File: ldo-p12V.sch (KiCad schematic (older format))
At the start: 8 parts

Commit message: change LDO sch capacitors & finish component selection
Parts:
- removed C?: 22u, symbol Device:C
- added C?: 4.7u, Capacitor_SMD:C_0805_2012Metric_Pad1.15x1.40mm_HandSolder, symbol Device:C
- C?: footprint (none) -> Capacitor_SMD:C_0805_2012Metric_Pad1.15x1.40mm_HandSolder; Description (none) -> CAP CER 10UF 16V X5R 0805; Manufacturer (none) -> Taiyo Yuden; Manufacturer Part Number (none) -> EMK212ABJ106KD-T; Supplier (none) -> Digi-Key; Supplier Part Number (none) -> 587-2980-1-ND
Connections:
- net +12Vreg: now also C?.2
- net GND: now also C?.1
- net at R?.2, U?.8 (SET): now also C?.2; no longer C?.2
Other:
- moved on the sheet: C?
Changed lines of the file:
@@
 L Device:C C?
 U 1 1 5CA5D41C
-P 4350 4400
+P 6650 4150
 AR Path="/5C87B3B6/5CA5D41C" Ref="C?"  Part="1"
 AR Path="/5CA59CF7/5CA5D41C" Ref="C?"  Part="1"
-F 0 "C?" H 4235 4354 50  0000 R CNN
-F 1 "10u" H 4235 4445 50  0000 R CNN
-F 2 "" H 4388 4250 50  0001 C CNN
-F 3 "" H 4350 4400 50  0001 C CNN
-F 4 "" H 1900 -750 50  0001 C CNN "Description"
-F 5 "" H 1900 -750 50  0001 C CNN "Manufacturer"
-F 6 "" H 1900 -750 50  0001 C CNN "Manufacturer Part Number"
-F 7 "" H 1900 -750 50  0001 C CNN "Supplier"
-F 8 "" H 1900 -750 50  0001 C CNN "Supplier Part Number"
-	1    4350 4400
-	1    0    0    1
+F 0 "C?" H 6535 4104 50  0000 R CNN
+F 1 "10u" H 6535 4195 50  0000 R CNN
+F 2 "Capacitor_SMD:C_0805_2012Metric_Pad1.15x1.40mm_HandSolder" H 6688 4000 50  0001 C CNN
+F 3 "https://www.yuden.co.jp/productdata/catalog/mlcc07_e.pdf" H 6650 4150 50  0001 C CNN
+F 4 "CAP CER 10UF 16V X5R 0805" H 4200 -1000 50  0001 C CNN "Description"
+F 5 "Taiyo Yuden" H 4200 -1000 50  0001 C CNN "Manufacturer"
+F 6 "EMK212ABJ106KD-T" H 4200 -1000 50  0001 C CNN "Manufacturer Part Number"
+F 7 "Digi-Key" H 4200 -1000 50  0001 C CNN "Supplier"
+F 8 "587-2980-1-ND" H 4200 -1000 50  0001 C CNN "Supplier Part Number"
+	1    6650 4150
+	-1   0    0    1
 $EndComp
 Wire Wire Line
@@
 Wire Wire Line
 	6450 4650 5500 4650
-$Comp
-L Device:C C?
-U 1 1 5CA5F77A
-P 6650 4150
-AR Path="/5C87B3B6/5CA5F77A" Ref="C?"  Part="1"
-AR Path="/5CA59CF7/5CA5F77A" Ref="C?"  Part="1"
-F 0 "C?" H 6535 4104 50  0000 R CNN
-F 1 "22u" H 6535 4195 50  0000 R CNN
-F 2 "" H 6688 4000 50  0001 C CNN
-F 3 "" H 6650 4150 50  0001 C CNN
-F 4 "" H 4200 -1000 50  0001 C CNN "Description"
-F 5 "" H 4200 -1000 50  0001 C CNN "Manufacturer"
-F 6 "" H 4200 -1000 50  0001 C CNN "Manufacturer Part Number"
-F 7 "" H 4200 -1000 50  0001 C CNN "Supplier"
-F 8 "" H 4200 -1000 50  0001 C CNN "Supplier Part Number"
-	1    6650 4150
-	-1   0    0    1
-$EndComp
 Wire Wire Line
 	6450 3650 6650 3650
@@
 	3950 4650 4350 4650
 Connection ~ 4350 4650
+$Comp
+L Device:C C?
+U 1 1 5D0393AC
+P 4350 4400
+AR Path="/5C87B3B6/5D0393AC" Ref="C?"  Part="1"
+AR Path="/5C903B7C/5D0393AC" Ref="C?"  Part="1"
+F 0 "C?" H 4235 4354 50  0000 R CNN
+F 1 "4.7u" H 4235 4445 50  0000 R CNN
+F 2 "Capacitor_SMD:C_0805_2012Metric_Pad1.15x1.40mm_HandSolder" H 4388 4250 50  0001 C CNN
+F 3 "https://www.yuden.co.jp/productdata/catalog/mlcc01_e.pdf" H 4350 4400 50  0001 C CNN
+F 4 "CAP CER 4.7UF 10V X5R 0805" H 1050 850 50  0001 C CNN "Description"
+F 5 "Taiyo Yuden" H 1050 850 50  0001 C CNN "Manufacturer"
+F 6 "LMK212BJ475KD-T" H 1050 850 50  0001 C CNN "Manufacturer Part Number"
+F 7 "Digi-Key" H 1050 850 50  0001 C CNN "Supplier"
+F 8 "587-1297-1-ND" H 1050 850 50  0001 C CNN "Supplier Part Number"
+	1    4350 4400
+	1    0    0    1
+$EndComp
 $EndSCHEMATC

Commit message: add components for audo.sch
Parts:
- R?: Description RES SMD 121K OHM 0.1% 1/8W 0805 Thin Film -> RES SMD 121K OHM 0.1% 1/8W 0805 Metal Film
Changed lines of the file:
@@
 F 2 "Resistor_SMD:R_0805_2012Metric_Pad1.15x1.40mm_HandSolder" V 4480 4400 50  0001 C CNN
 F 3 "https://industrial.panasonic.com/cdbs/www-data/pdf/RDM0000/AOA0000C307.pdf" H 4550 4400 50  0001 C CNN
-F 4 "RES SMD 121K OHM 0.1% 1/8W 0805 Thin Film" H 4550 4400 50  0001 C CNN "Description"
+F 4 "RES SMD 121K OHM 0.1% 1/8W 0805 Metal Film" H 4550 4400 50  0001 C CNN "Description"
 F 5 "Panasonic Electronic Components" H 4550 4400 50  0001 C CNN "Manufacturer"
 F 6 "ERA-6AEB1213V" H 4550 4400 50  0001 C CNN "Manufacturer Part Number"

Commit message: switch components supplier to Mouser for price/availability
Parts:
- C?: Supplier Digi-Key -> Mouser; Supplier Part Number 587-1297-1-ND -> 963-LMK212BJ475KD-T
- U?: Supplier Digi-Key -> Mouser; Supplier Part Number LT3045EMSE#PBF-ND -> 584-LT3045EMSE#PBF
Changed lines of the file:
@@
 F 5 "Linear Technology" H 0   0   50  0001 C CNN "Manufacturer"
 F 6 "LT3045EMSE#PBF" H 0   0   50  0001 C CNN "Manufacturer Part Number"
-F 7 "Digi-Key" H 0   0   50  0001 C CNN "Supplier"
-F 8 "LT3045EMSE#PBF-ND" H 0   0   50  0001 C CNN "Supplier Part Number"
+F 7 "Mouser" H 0   0   50  0001 C CNN "Supplier"
+F 8 "584-LT3045EMSE#PBF" H 0   0   50  0001 C CNN "Supplier Part Number"
 	1    5500 3900
 	1    0    0    -1
@@
 F 5 "Taiyo Yuden" H 1050 850 50  0001 C CNN "Manufacturer"
 F 6 "LMK212BJ475KD-T" H 1050 850 50  0001 C CNN "Manufacturer Part Number"
-F 7 "Digi-Key" H 1050 850 50  0001 C CNN "Supplier"
-F 8 "587-1297-1-ND" H 1050 850 50  0001 C CNN "Supplier Part Number"
+F 7 "Mouser" H 1050 850 50  0001 C CNN "Supplier"
+F 8 "963-LMK212BJ475KD-T" H 1050 850 50  0001 C CNN "Supplier Part Number"
 	1    4350 4400
 	1    0    0    1

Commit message: update ldo threshold configs & components
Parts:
- R?: value 1.82M -> 1.91M; Description RES SMD 1.82M OHM 1% 1/8W 0805 -> RES SMD 1.91M OHM 1% 1/8W 0805; Manufacturer Part Number ERJ-6ENF1824V -> ERJ-6ENF1914V; Supplier Part Number P1.82BTCT-ND -> P1.91BTCT-ND
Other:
- note added: "LT3045 keeps IC in shutdown while EN is below 1.24V\n—> V_EN_threshold = 1.24V*(1+(432k/49.9k)) = 11.975V\n\nLT3045 fast start-up circuitry increases SET pin\ncurrent to ~~2mA while PGFB is below 300mV.\n—> V_PG_threshold = 0.3V*(1+(1.91M/49.9k)) = 11.78V"
- note removed: "NOTE: LT3045’s fast start-up circuitry increases the\nSET pin current to ~2mA while PGFB is below 300mV."
- note removed: "R_PG values of 1.13M & 29.4k yield fast start-up lasting ~~50ms"
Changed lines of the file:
@@
 AR Path="/5CA59CF7/5CA5DDF4" Ref="R?"  Part="1"
 F 0 "R?" V 6530 3900 50  0000 C CNN
-F 1 "1.82M" V 6450 3900 50  0000 C CNN
+F 1 "1.91M" V 6450 3900 50  0000 C CNN
 F 2 "Resistor_SMD:R_0805_2012Metric_Pad1.15x1.40mm_HandSolder" V 6380 3900 50  0001 C CNN
 F 3 "https://industrial.panasonic.com/cdbs/www-data/pdf/RDA0000/AOA0000C304.pdf" H 6450 3900 50  0001 C CNN
-F 4 "RES SMD 1.82M OHM 1% 1/8W 0805" H 6450 3900 50  0001 C CNN "Description"
+F 4 "RES SMD 1.91M OHM 1% 1/8W 0805" H 6450 3900 50  0001 C CNN "Description"
 F 5 "Panasonic Electronic Components" H 6450 3900 50  0001 C CNN "Manufacturer"
-F 6 "ERJ-6ENF1824V" H 6450 3900 50  0001 C CNN "Manufacturer Part Number"
+F 6 "ERJ-6ENF1914V" H 6450 3900 50  0001 C CNN "Manufacturer Part Number"
 F 7 "Digi-Key" H 6450 3900 50  0001 C CNN "Supplier"
-F 8 "P1.82BTCT-ND" H 6450 3900 50  0001 C CNN "Supplier Part Number"
+F 8 "P1.91BTCT-ND" H 6450 3900 50  0001 C CNN "Supplier Part Number"
 	1    6450 3900
 	-1   0    0    1
@@
 	6850 3650 6650 3650
 Connection ~ 6650 3650
-Text Notes 3900 5400 0    50   ~ 0
-NOTE: LT3045’s fast start-up circuitry increases the\nSET pin current to ~2mA while PGFB is below 300mV.
-Text Notes 3900 5550 0    50   ~ 0
-R_PG values of 1.13M & 29.4k yield fast start-up lasting ~~50ms
+Text Notes 3950 3450 0    50   ~ 0
+LT3045 keeps IC in shutdown while EN is below 1.24V\n—> V_EN_threshold = 1.24V*(1+(432k/49.9k)) = 11.975V\n\nLT3045 fast start-up circuitry increases SET pin\ncurrent to ~~2mA while PGFB is below 300mV.\n—> V_PG_threshold = 0.3V*(1+(1.91M/49.9k)) = 11.78V
 $Comp
 L Device:R R?

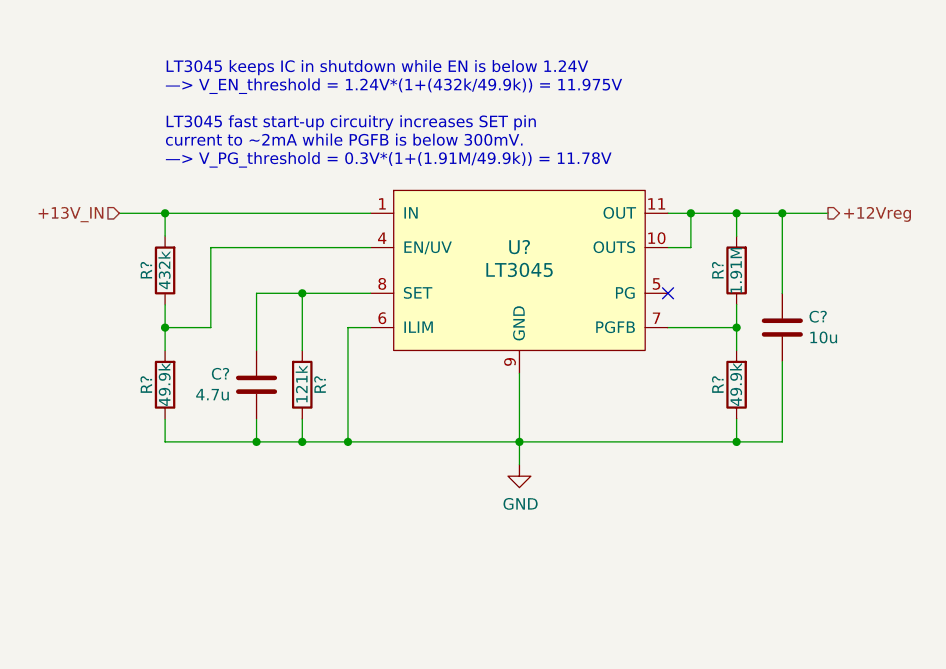
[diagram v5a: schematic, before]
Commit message: fix audio pot label & other label sizing
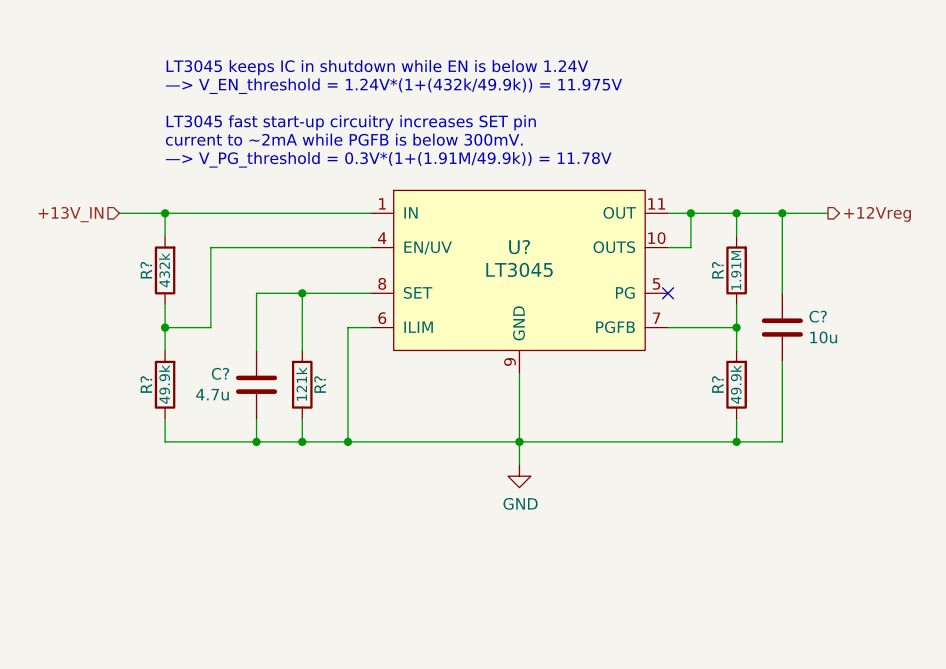
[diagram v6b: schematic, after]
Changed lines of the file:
@@
 AR Path="/5CA59CF7/5CA5D410" Ref="R?"  Part="1"
 F 0 "R?" V 4630 4400 50  0000 C CNN
-F 1 "121k" V 4550 4400 50  0000 C CNN
+F 1 "121k" V 4550 4400 45  0000 C CNN
 F 2 "Resistor_SMD:R_0805_2012Metric_Pad1.15x1.40mm_HandSolder" V 4480 4400 50  0001 C CNN
 F 3 "https://industrial.panasonic.com/cdbs/www-data/pdf/RDM0000/AOA0000C307.pdf" H 4550 4400 50  0001 C CNN
@@
 AR Path="/5CA59CF7/5CA5DD37" Ref="R?"  Part="1"
 F 0 "R?" V 6530 4400 50  0000 C CNN
-F 1 "49.9k" V 6450 4400 50  0000 C CNN
+F 1 "49.9k" V 6450 4400 45  0000 C CNN
 F 2 "Resistor_SMD:R_0805_2012Metric_Pad1.15x1.40mm_HandSolder" V 6380 4400 50  0001 C CNN
 F 3 "https://industrial.panasonic.com/cdbs/www-data/pdf/RDA0000/AOA0000C304.pdf" H 6450 4400 50  0001 C CNN
@@
 AR Path="/5CA59CF7/5CA5DDF4" Ref="R?"  Part="1"
 F 0 "R?" V 6530 3900 50  0000 C CNN
-F 1 "1.91M" V 6450 3900 50  0000 C CNN
+F 1 "1.91M" V 6450 3900 43  0000 C CNN
 F 2 "Resistor_SMD:R_0805_2012Metric_Pad1.15x1.40mm_HandSolder" V 6380 3900 50  0001 C CNN
 F 3 "https://industrial.panasonic.com/cdbs/www-data/pdf/RDA0000/AOA0000C304.pdf" H 6450 3900 50  0001 C CNN
@@
 AR Path="/5CA59CF7/5CAC0D09" Ref="R?"  Part="1"
 F 0 "R?" V 4030 4400 50  0000 C CNN
-F 1 "49.9k" V 3950 4400 50  0000 C CNN
+F 1 "49.9k" V 3950 4400 45  0000 C CNN
 F 2 "Resistor_SMD:R_0805_2012Metric_Pad1.15x1.40mm_HandSolder" V 3880 4400 50  0001 C CNN
 F 3 "https://industrial.panasonic.com/cdbs/www-data/pdf/RDA0000/AOA0000C304.pdf" H 3950 4400 50  0001 C CNN
@@
 AR Path="/5CA59CF7/5CAC0D15" Ref="R?"  Part="1"
 F 0 "R?" V 4030 3900 50  0000 C CNN
-F 1 "432k" V 3950 3900 50  0000 C CNN
+F 1 "432k" V 3950 3900 45  0000 C CNN
 F 2 "Resistor_SMD:R_0805_2012Metric_Pad1.15x1.40mm_HandSolder" V 3880 3900 50  0001 C CNN
 F 3 "https://industrial.panasonic.com/cdbs/www-data/pdf/RDA0000/AOA0000C304.pdf" H 3950 3900 50  0001 C CNN

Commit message: add circuit notes
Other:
- note added: "LT3045 keeps IC in shutdown while EN is below 1.24V\n—> V_EN_threshold = 1.24V*(1+(432k/49.9k)) = 11.975V\n\nLT3045 fast start-up circuitry increases SET pin\ncurrent to ~~2mA while PGFB is below 300mV.\n—> V_PG_threshold = 0.3V*(1+(1.91M/49.9k)) = 11.78V\n\nV_o = I_SET * R_SET = 100uA * 121k = 12.1V"
- note removed: "LT3045 keeps IC in shutdown while EN is below 1.24V\n—> V_EN_threshold = 1.24V*(1+(432k/49.9k)) = 11.975V\n\nLT3045 fast start-up circuitry increases SET pin\ncurrent to ~~2mA while PGFB is below 300mV.\n—> V_PG_threshold = 0.3V*(1+(1.91M/49.9k)) = 11.78V"
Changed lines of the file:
@@
 Connection ~ 6650 3650
 Text Notes 3950 3450 0    50   ~ 0
-LT3045 keeps IC in shutdown while EN is below 1.24V\n—> V_EN_threshold = 1.24V*(1+(432k/49.9k)) = 11.975V\n\nLT3045 fast start-up circuitry increases SET pin\ncurrent to ~~2mA while PGFB is below 300mV.\n—> V_PG_threshold = 0.3V*(1+(1.91M/49.9k)) = 11.78V
+LT3045 keeps IC in shutdown while EN is below 1.24V\n—> V_EN_threshold = 1.24V*(1+(432k/49.9k)) = 11.975V\n\nLT3045 fast start-up circuitry increases SET pin\ncurrent to ~~2mA while PGFB is below 300mV.\n—> V_PG_threshold = 0.3V*(1+(1.91M/49.9k)) = 11.78V\n\nV_o = I_SET * R_SET = 100uA * 121k = 12.1V
 $Comp
 L Device:R R?
